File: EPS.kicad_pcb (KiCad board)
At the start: 6 copper layers, 205.4 x 95.8 mm, 83 parts, among them J801 Battery_1, Q2701 IRLML5103, Q3301 NMOS, Q3302 NMOS, Q801 NMOS, Q802 NMOS, U2701 ADA4807-1, U3301 LM74700, U3302 LM74700, U3303 TMCS1101A2UQDT, U3501 AP22653AW6-7, U3502 AP22653AW6-7, U801 BQ76920PW

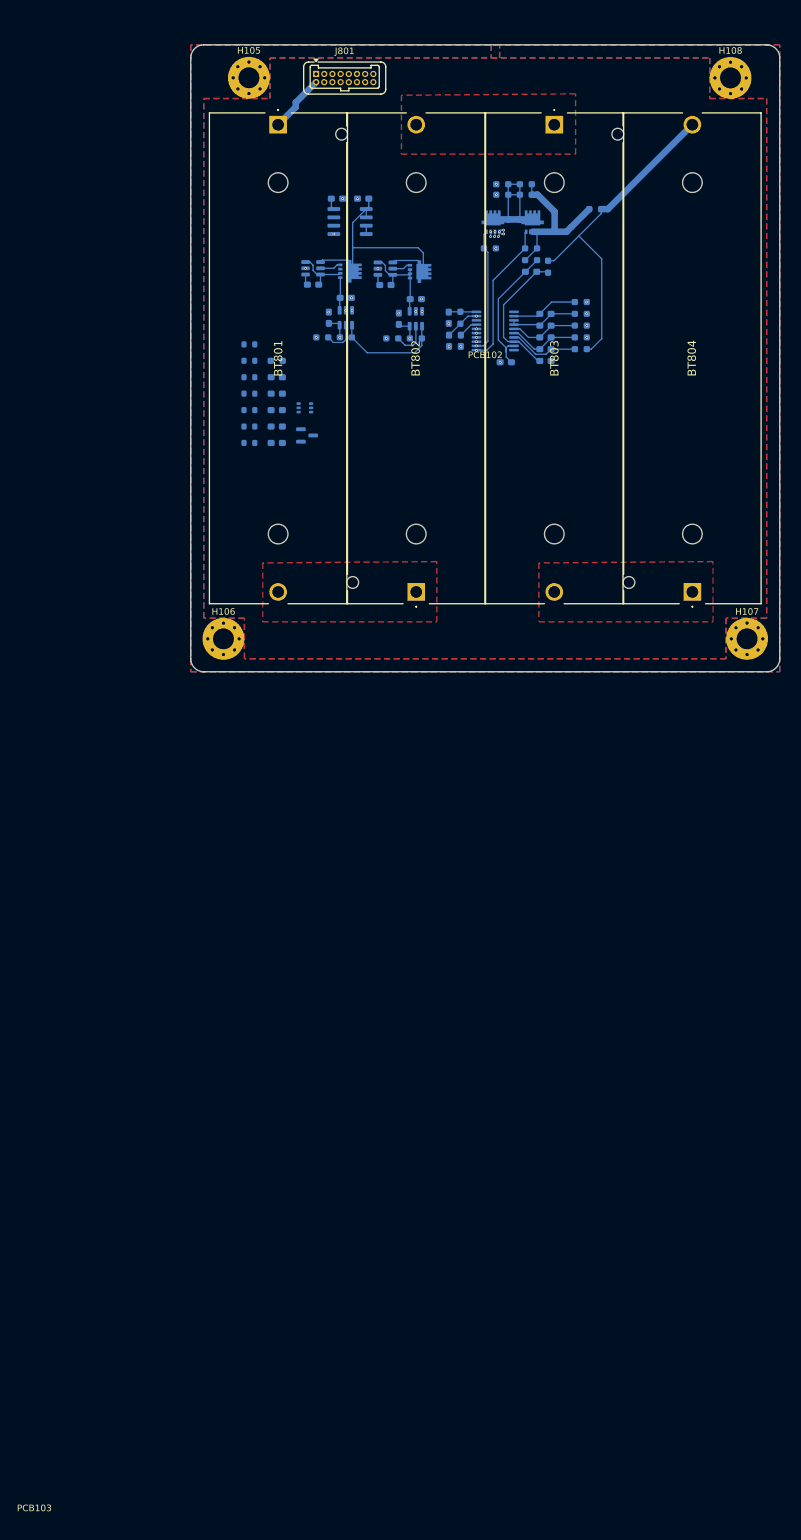
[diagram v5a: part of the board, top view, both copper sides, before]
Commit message: added values to most parts
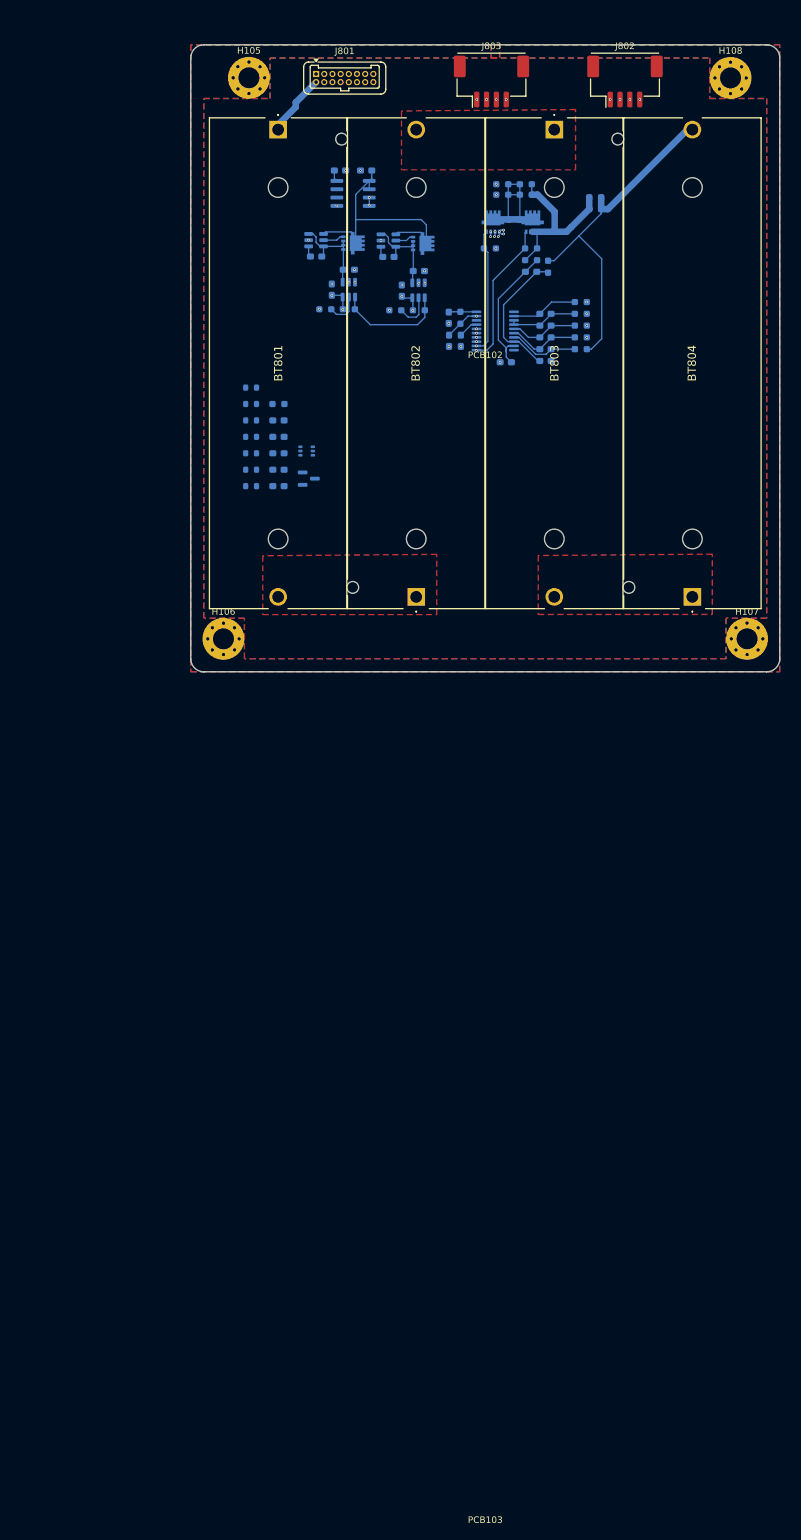
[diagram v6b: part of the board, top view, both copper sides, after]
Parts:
- added J802: HEATER_CONN, Connector_Molex:Molex_CLIK-Mate_505405-0470_1x04-1MP_P1.50mm_Vertical, F.Cu at (106.0, 47.7)
- added J803: HEATER_CONN, Connector_Molex:Molex_CLIK-Mate_505405-0470_1x04-1MP_P1.50mm_Vertical, F.Cu at (85.5, 47.7)
- added R816: 0R, Resistor_SMD:R_0603_1608Metric_Pad0.98x0.95mm_HandSolder, B.Cu at (101.4, 65.4)
- C806: value C_Small -> 1uF
- C807, C808, C810: value 1uF -> 100n
- C809: value C_Small -> 10uF
- R3503, R3504: value R_Small -> SELECT
- R801, R802, R803, R804, R805, R806, R808, R809: value R_Small -> 100
- R807: value R_Small -> 20m
- R810, R815: value R_Small -> 1M
- moved PCB103 68.9 mm to (84.6, 268.0)
- moved C2703 6.61 mm to (53.0, 104.5)
- moved Q2701 6.61 mm to (57.6, 108.4)
- moved R2701 6.61 mm to (53.0, 97.0)
- moved R2704 6.61 mm to (48.8, 104.5)
- moved R2707 6.61 mm to (48.8, 97.0)
- moved U2701 6.61 mm to (57.3, 104.2)
- moved C2701 6.61 mm to (53.0, 109.5)
- moved C2702 6.61 mm to (53.0, 107.0)
- moved C2704 6.61 mm to (53.0, 102.0)
- moved C2705 6.61 mm to (53.0, 99.5)
- moved R2702 6.61 mm to (48.8, 109.5)
- moved R2703 6.61 mm to (48.8, 107.0)
- moved R2705 6.61 mm to (48.8, 102.0)
- moved R2706 6.61 mm to (48.8, 99.5)
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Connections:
- net /Battery_Input_1/BATT_ALERT renamed /BATT_ALERT_1
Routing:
- net Net-(Q801-S): track 26.2 -> 28.0 mm
- net /Battery_Input_1/BATT_0: track 51.2 -> 53.0 mm
- net /Battery_Input_1/Switch_Batt_Heater/Switch_element/VOUT2: track 13.3 -> 14.6 mm
- net /Battery_Input_1/Pack: vias 4 -> 6
- net GND: vias 31 -> 35
- net /Battery_Input_1/Switch_Batt_Heater/VOUT: vias 0 -> 6

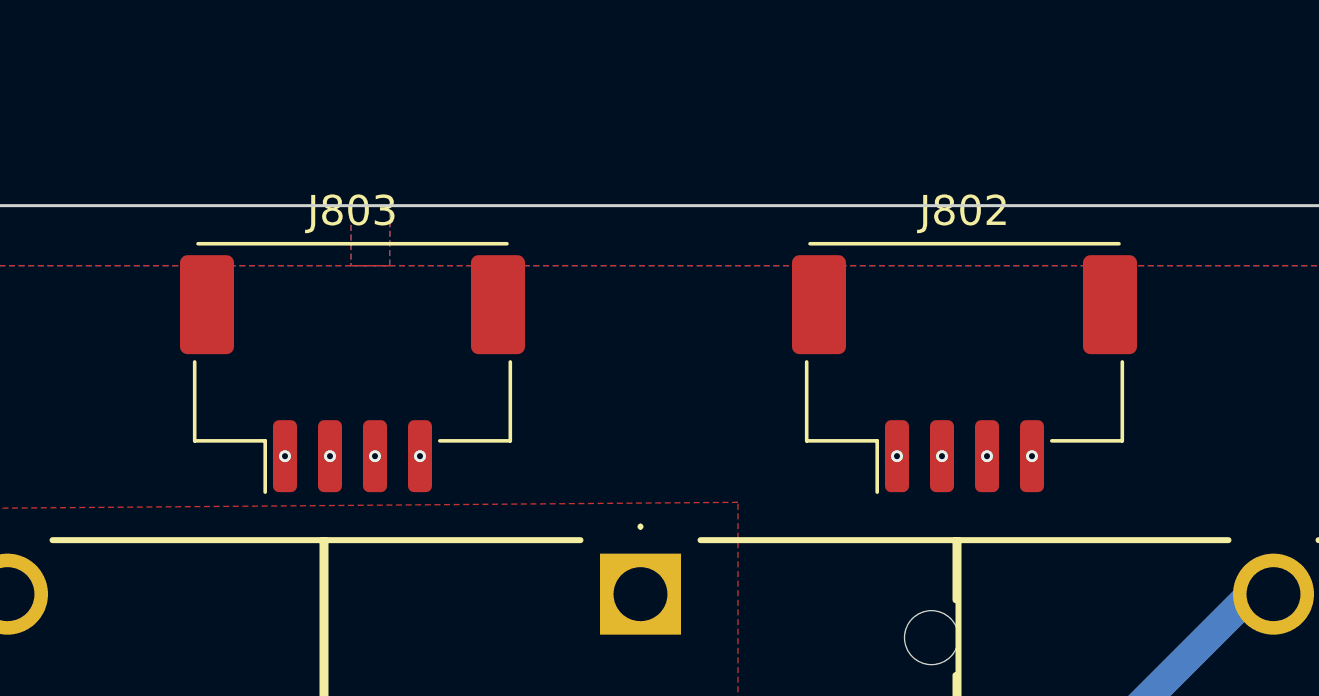
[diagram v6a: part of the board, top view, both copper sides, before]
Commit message: added missing heater connectors
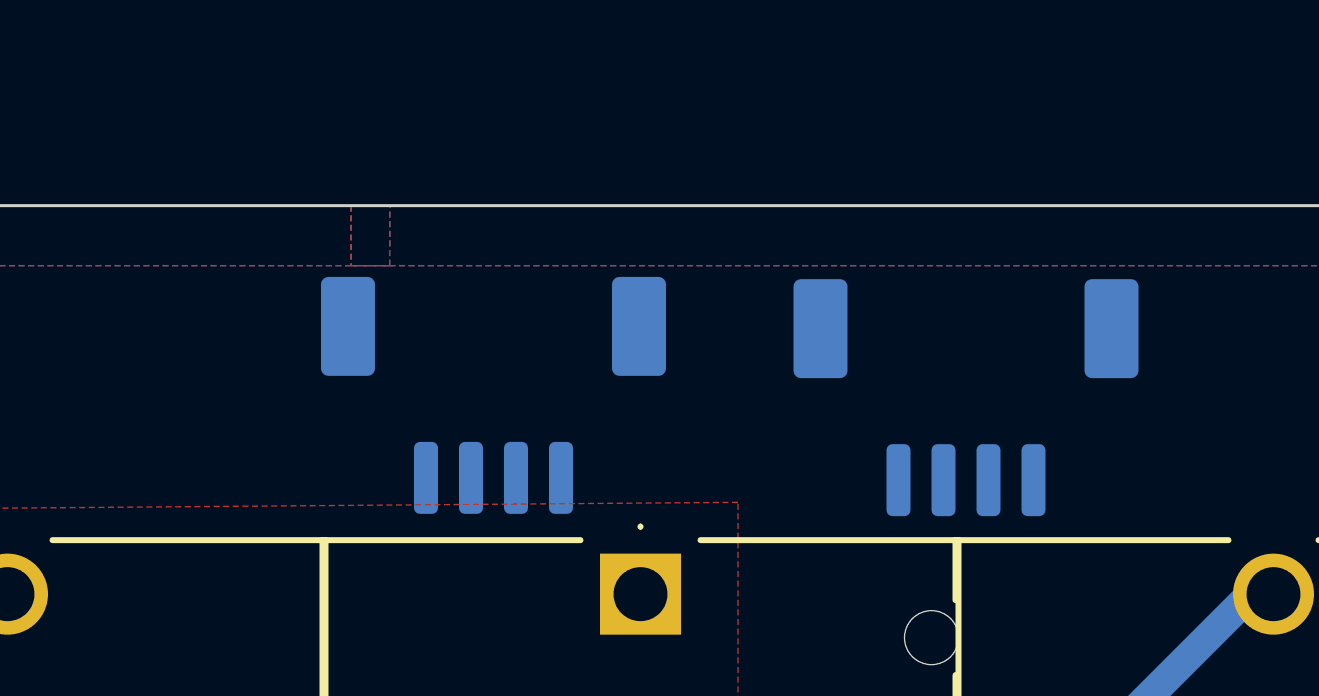
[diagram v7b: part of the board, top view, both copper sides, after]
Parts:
- J802, J803: moved to B.Cu
- moved J803 4.76 mm to (90.2, 48.4), turned to 180 degrees
- moved J802 0.80 mm to (106.0, 48.5), turned to 180 degrees
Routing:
- net GND: vias 35 -> 31
- net /Battery_Input_1/Switch_Batt_Heater/VOUT: vias 6 -> 2

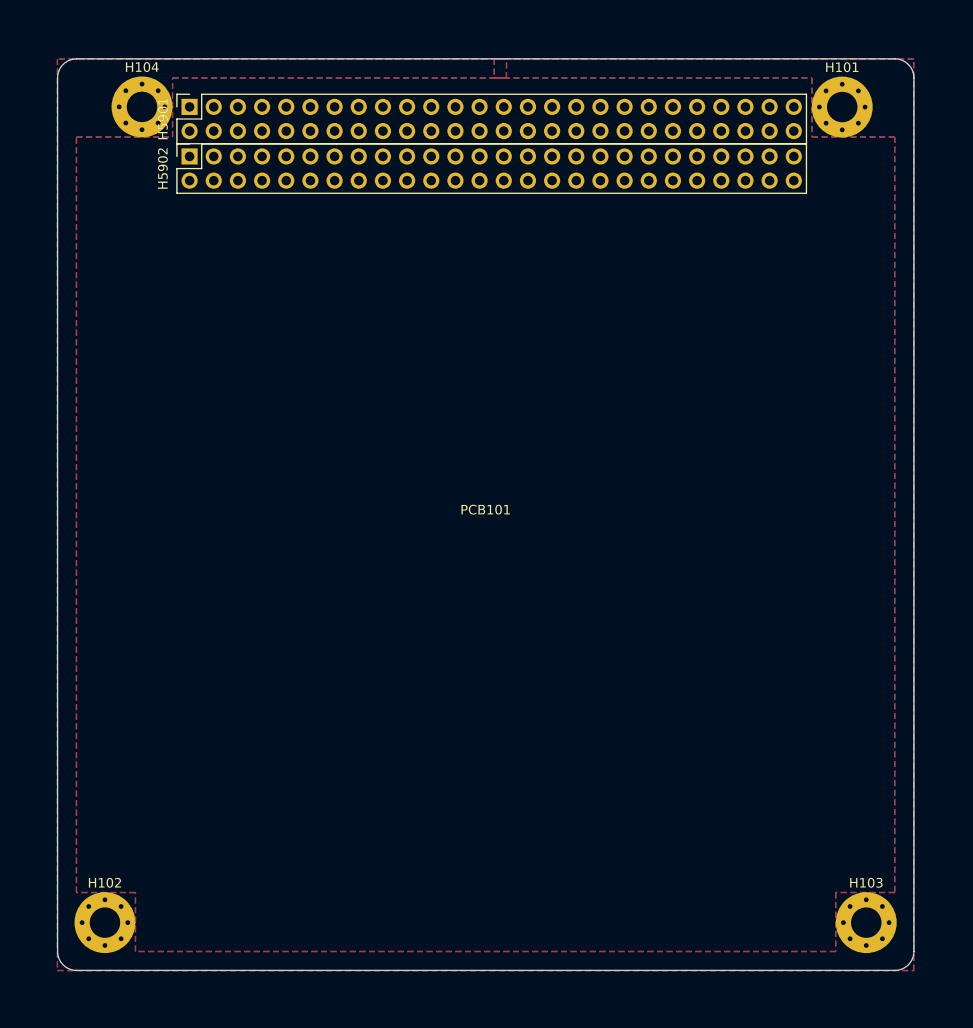
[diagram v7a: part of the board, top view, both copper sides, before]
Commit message: replaced individual CC sourses for SOL with a single one
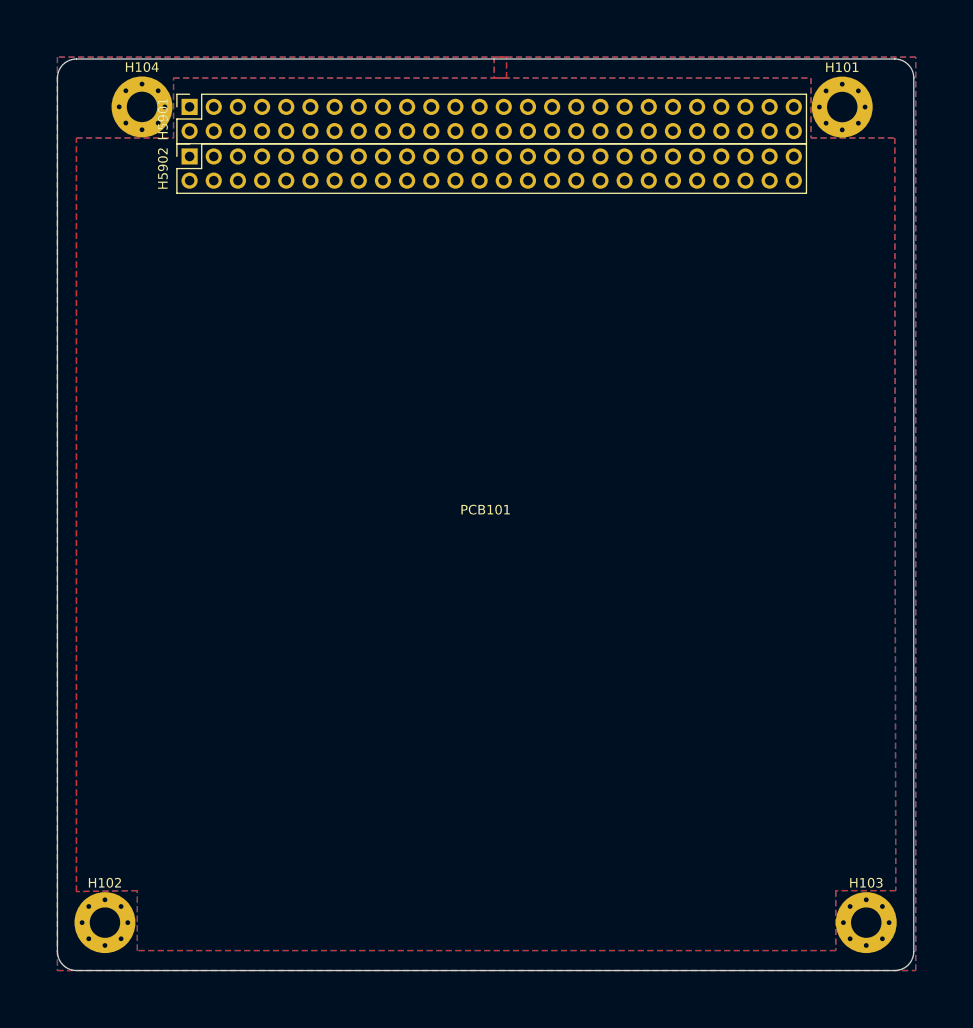
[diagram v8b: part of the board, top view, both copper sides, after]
